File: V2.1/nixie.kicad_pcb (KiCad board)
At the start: 4 copper layers, 182.5 x 68.3 mm, 66 parts, among them IC1 K155ID1, IC10 TPS54302DDCT, IC2 SN74141, IC3 K155ID1, IC4 K155ID1, IC5 MCP23017-E_SO, IC6 DS3231M+TRL, IC7 K155ID1, IC8 K155ID1, J1 M20-9990446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

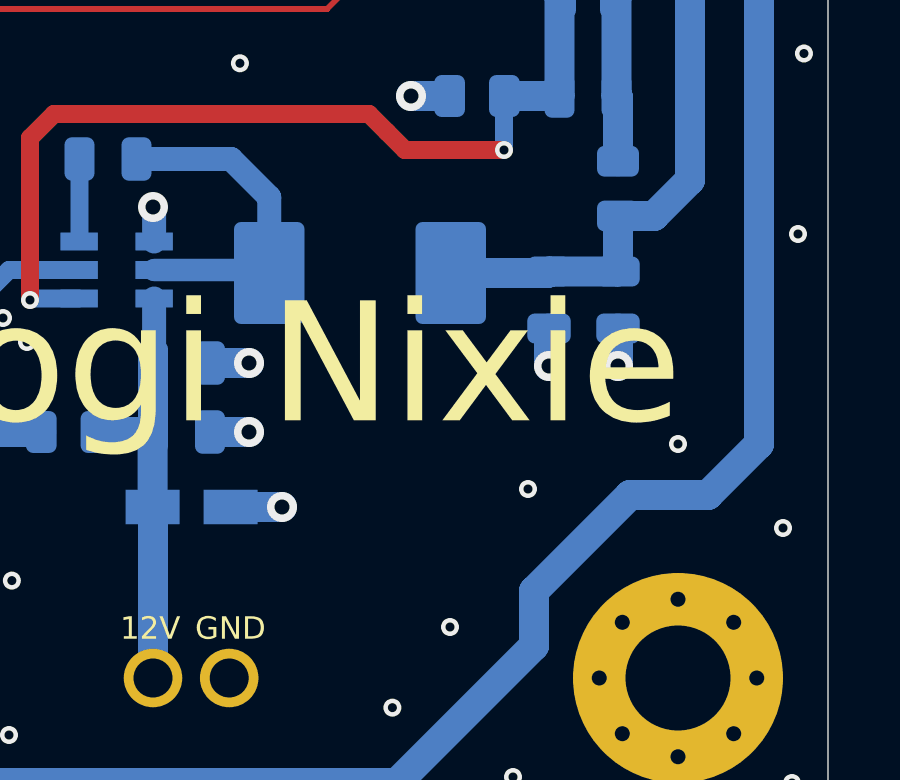
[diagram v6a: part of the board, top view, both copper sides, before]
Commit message: Added a few extra vias
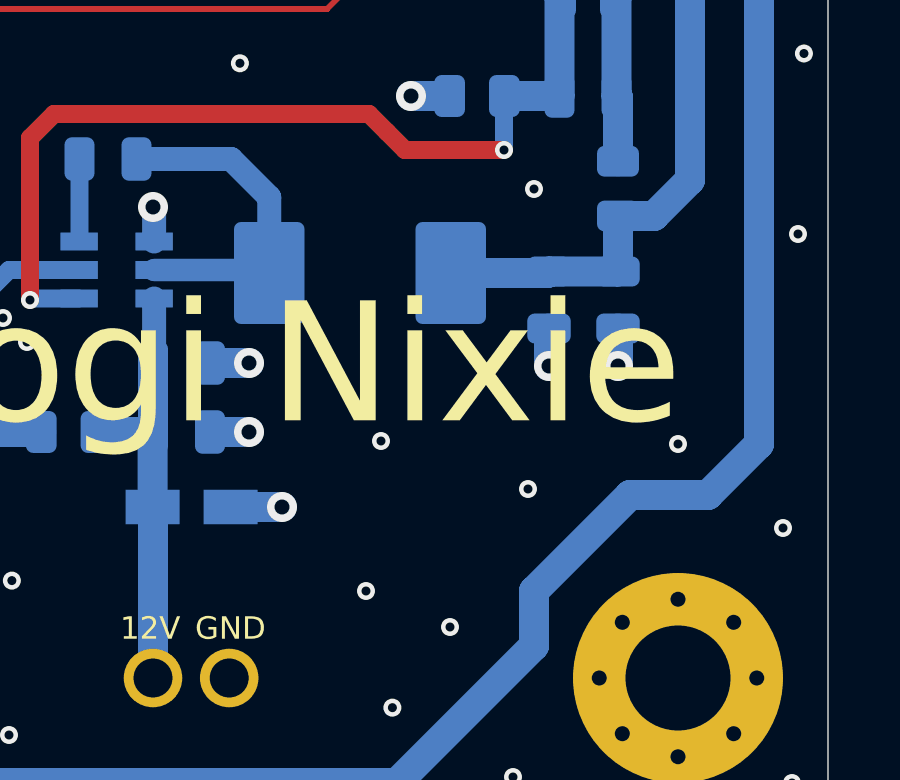
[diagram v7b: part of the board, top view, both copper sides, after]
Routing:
- net GND: vias 289 -> 292
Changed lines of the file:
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@@
   (via (at 141.9 131.4) (size 0.6) (drill 0.3) (layers "F.Cu" "B.Cu") (net 2))
   (via (at 145.2 133.5) (size 0.6) (drill 0.3) (layers "F.Cu" "B.Cu") (free) (net 2))
+  (via (at 237.7 124.8) (size 0.6) (drill 0.3) (layers "F.Cu" "B.Cu") (free) (net 2))
   (via (at 137.9 98.6) (size 0.6) (drill 0.3) (layers "F.Cu" "B.Cu") (free) (net 2))
   (via (at 180.595791 103.589038) (size 0.6) (drill 0.3) (layers "F.Cu" "B.Cu") (free) (net 2))
@@
   (via (at 218.7 122.2) (size 0.6) (drill 0.3) (layers "F.Cu" "B.Cu") (free) (net 2))
   (via (at 119.186374 117.543187) (size 0.6) (drill 0.3) (layers "F.Cu" "B.Cu") (free) (net 2))
+  (via (at 232.6 133.2) (size 0.6) (drill 0.3) (layers "F.Cu" "B.Cu") (free) (net 2))
   (via (at 236.7 79.2) (size 0.6) (drill 0.3) (layers "F.Cu" "B.Cu") (free) (net 2))
   (via (at 204.9 115.1) (size 0.6) (drill 0.3) (layers "F.Cu" "B.Cu") (free) (net 2))
@@
   (via (at 182.2 87.7) (size 0.6) (drill 0.3) (layers "F.Cu" "B.Cu") (free) (net 2))
   (via (at 110.4 107.4) (size 1) (drill 0.5) (layers "F.Cu" "B.Cu") (net 2))
+  (via (at 232.1 138.2) (size 0.6) (drill 0.3) (layers "F.Cu" "B.Cu") (free) (net 2))
   (via (at 120.5 87.6) (size 0.6) (drill 0.3) (layers "F.Cu" "B.Cu") (free) (net 2))
   (via (at 66.1 121.1) (size 0.6) (drill 0.3) (layers "F.Cu" "B.Cu") (free) (net 2))

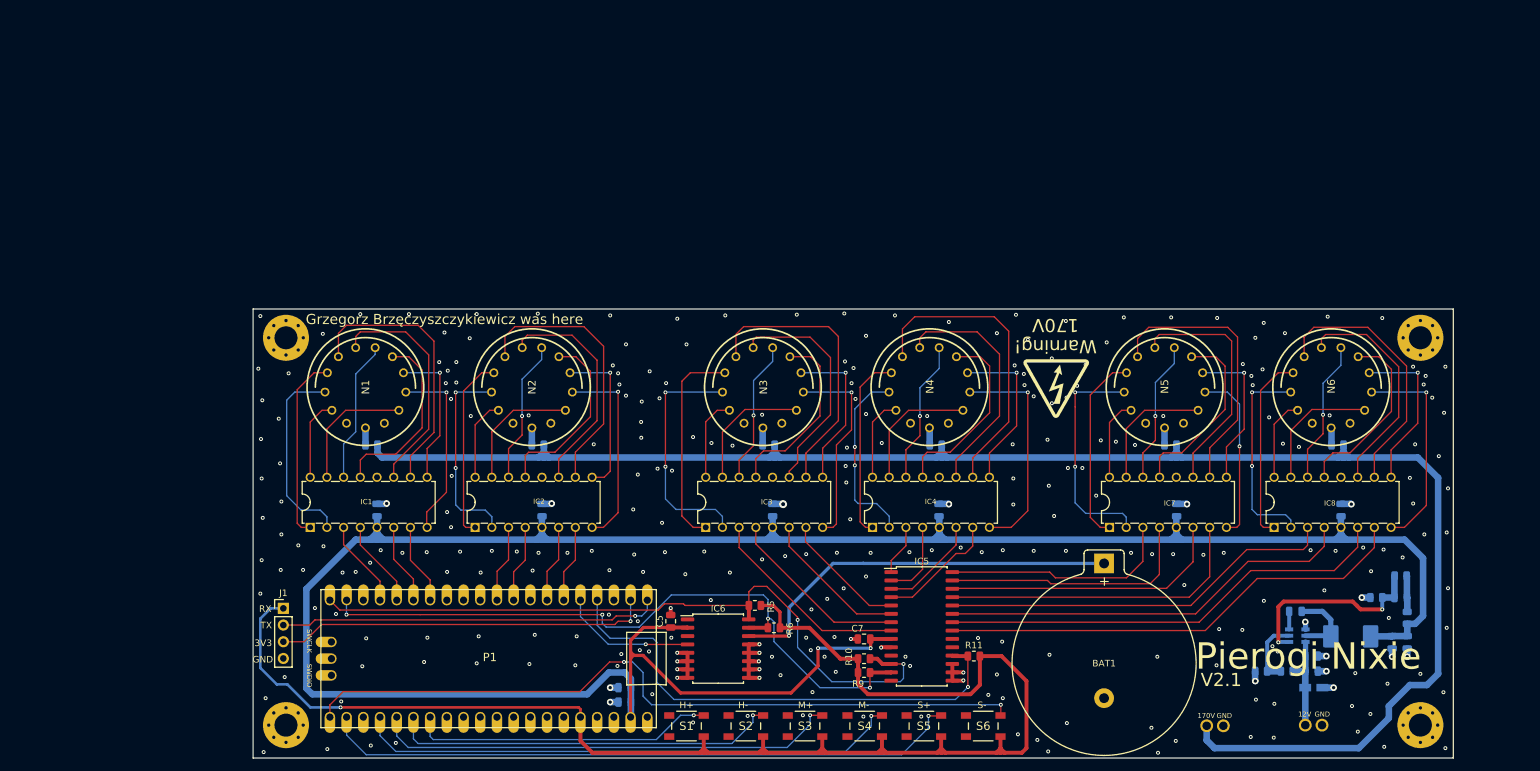
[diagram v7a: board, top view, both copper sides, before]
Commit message: Updated bom, slightchanges to footprint indicators
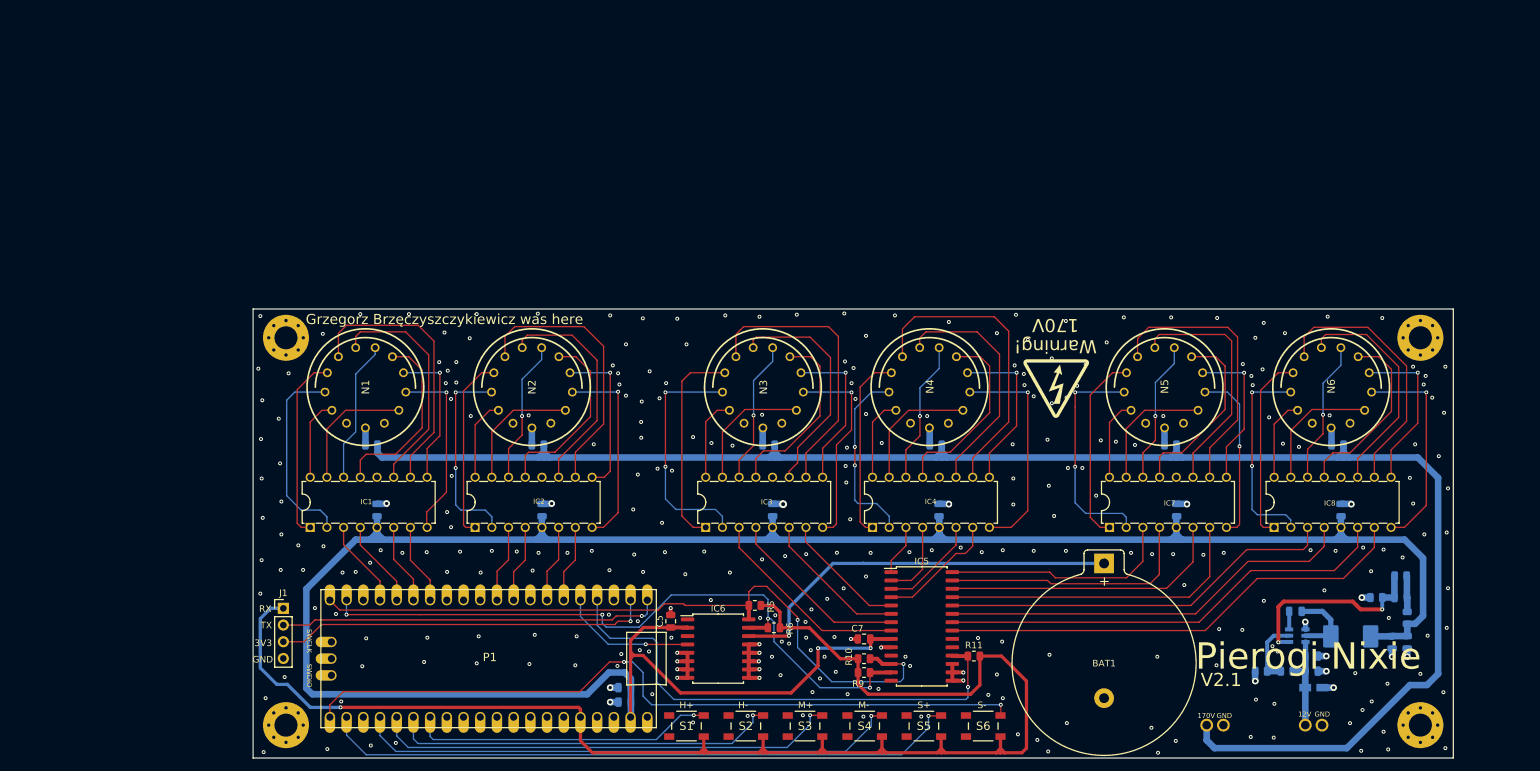
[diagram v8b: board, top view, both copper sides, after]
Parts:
- IC2: value SN74141 -> K155ID1
- moved U$3 3.81 mm to (177.7, 130.5)
- moved J3 0.10 mm to (210.0, 141.1)
- renumbered C18 to C17, IC10 to IC9
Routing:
- net VCC: track 258.3 -> 257.4 mm
- net /RSTIO: track 76.3 -> 77.3 mm
- net GND: vias 292 -> 305
